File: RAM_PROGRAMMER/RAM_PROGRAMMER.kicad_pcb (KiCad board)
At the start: 4 copper layers, 149.1 x 66 mm, 60 parts, among them J1 Conn_01x02, J2 Conn_01x08, J3 Conn_01x08, J4 Conn_01x08, J5 Conn_01x02, J6 Conn_01x04, J7 Conn_01x11, SW1 SW_Push, U1 ATmega328-PU, U10 74LS245, U2 IS61C1024-15N, U3 74HC595, U4 74LS245, U5 74HC595, U6 74LS157, U7 74LS157, U8 74LS157, U9 74LS157, Y1 Crystal

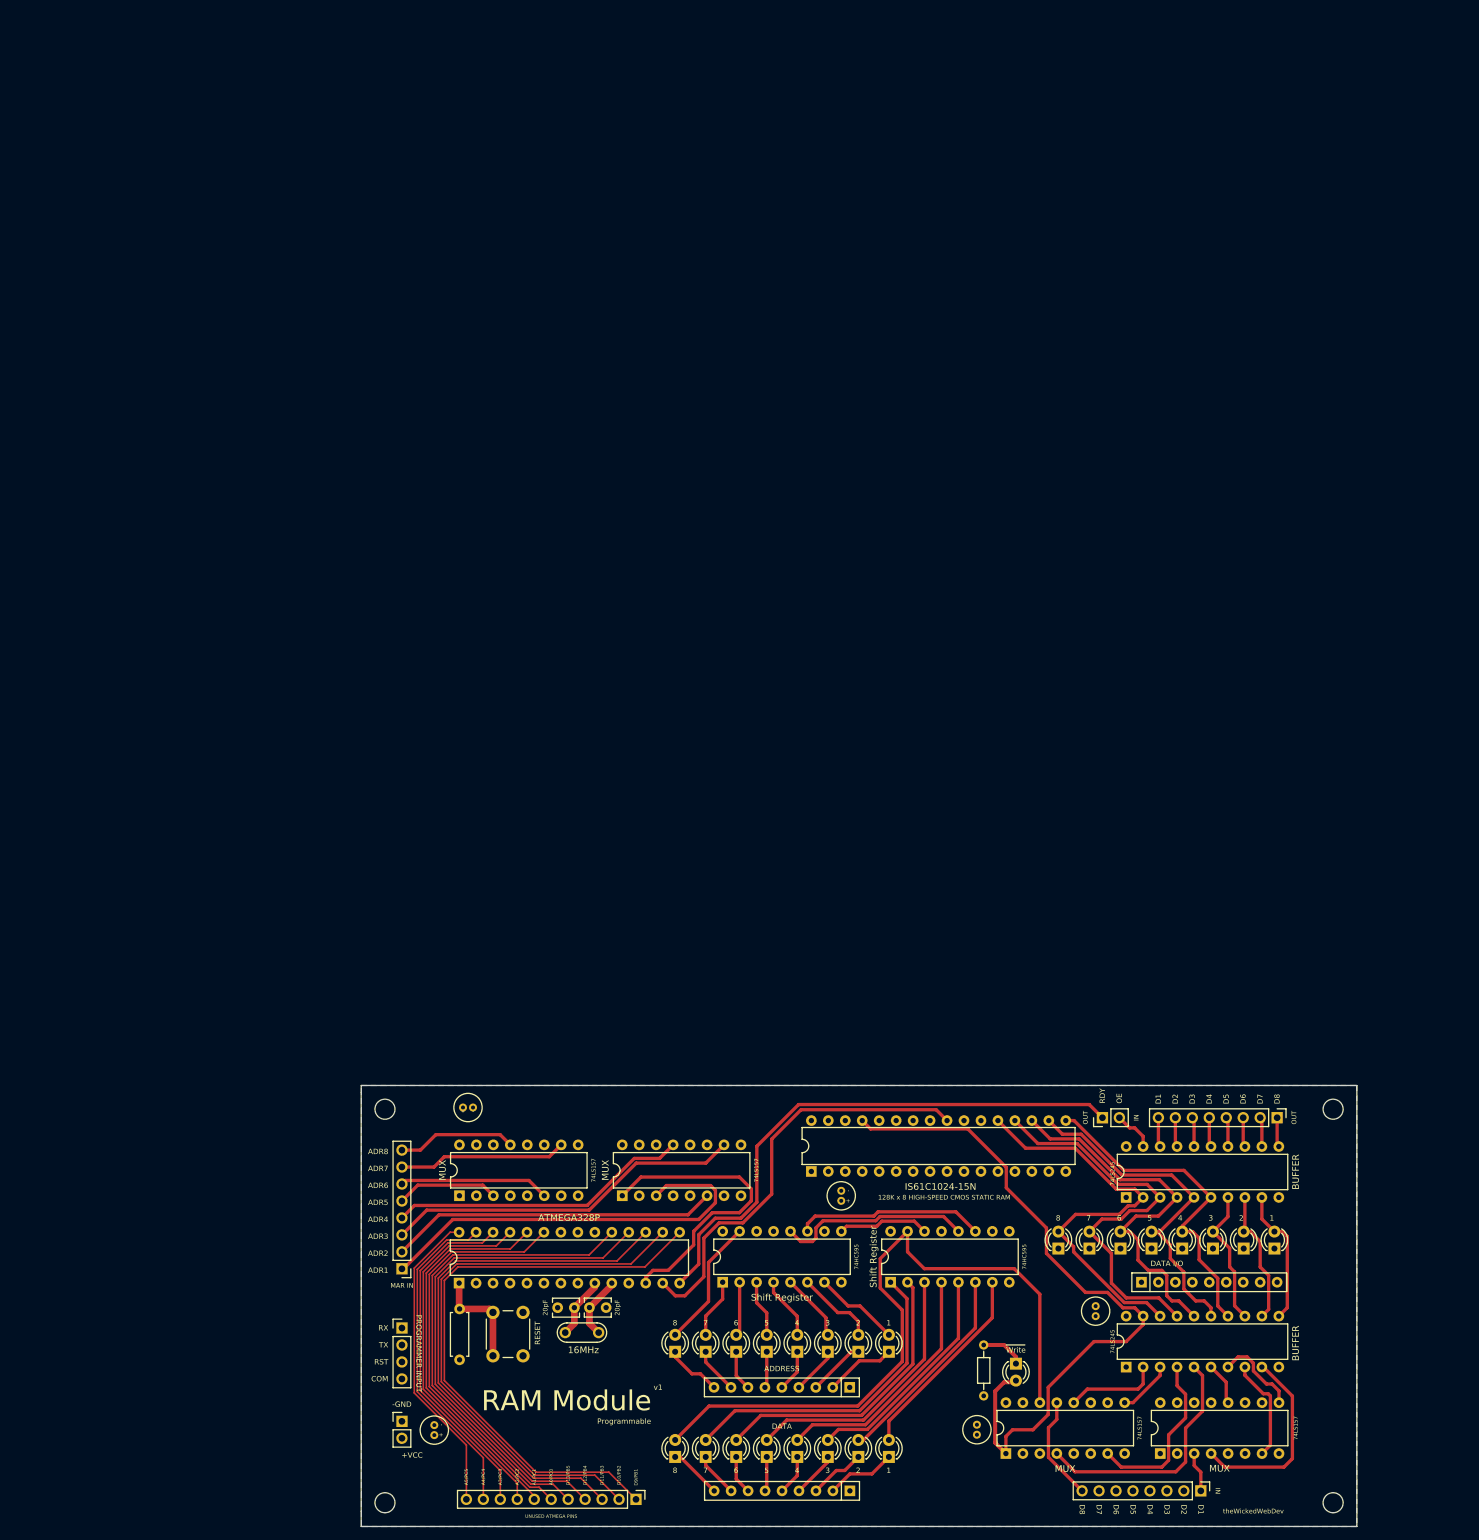
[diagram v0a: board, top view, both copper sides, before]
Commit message: Added RAM Programmer module
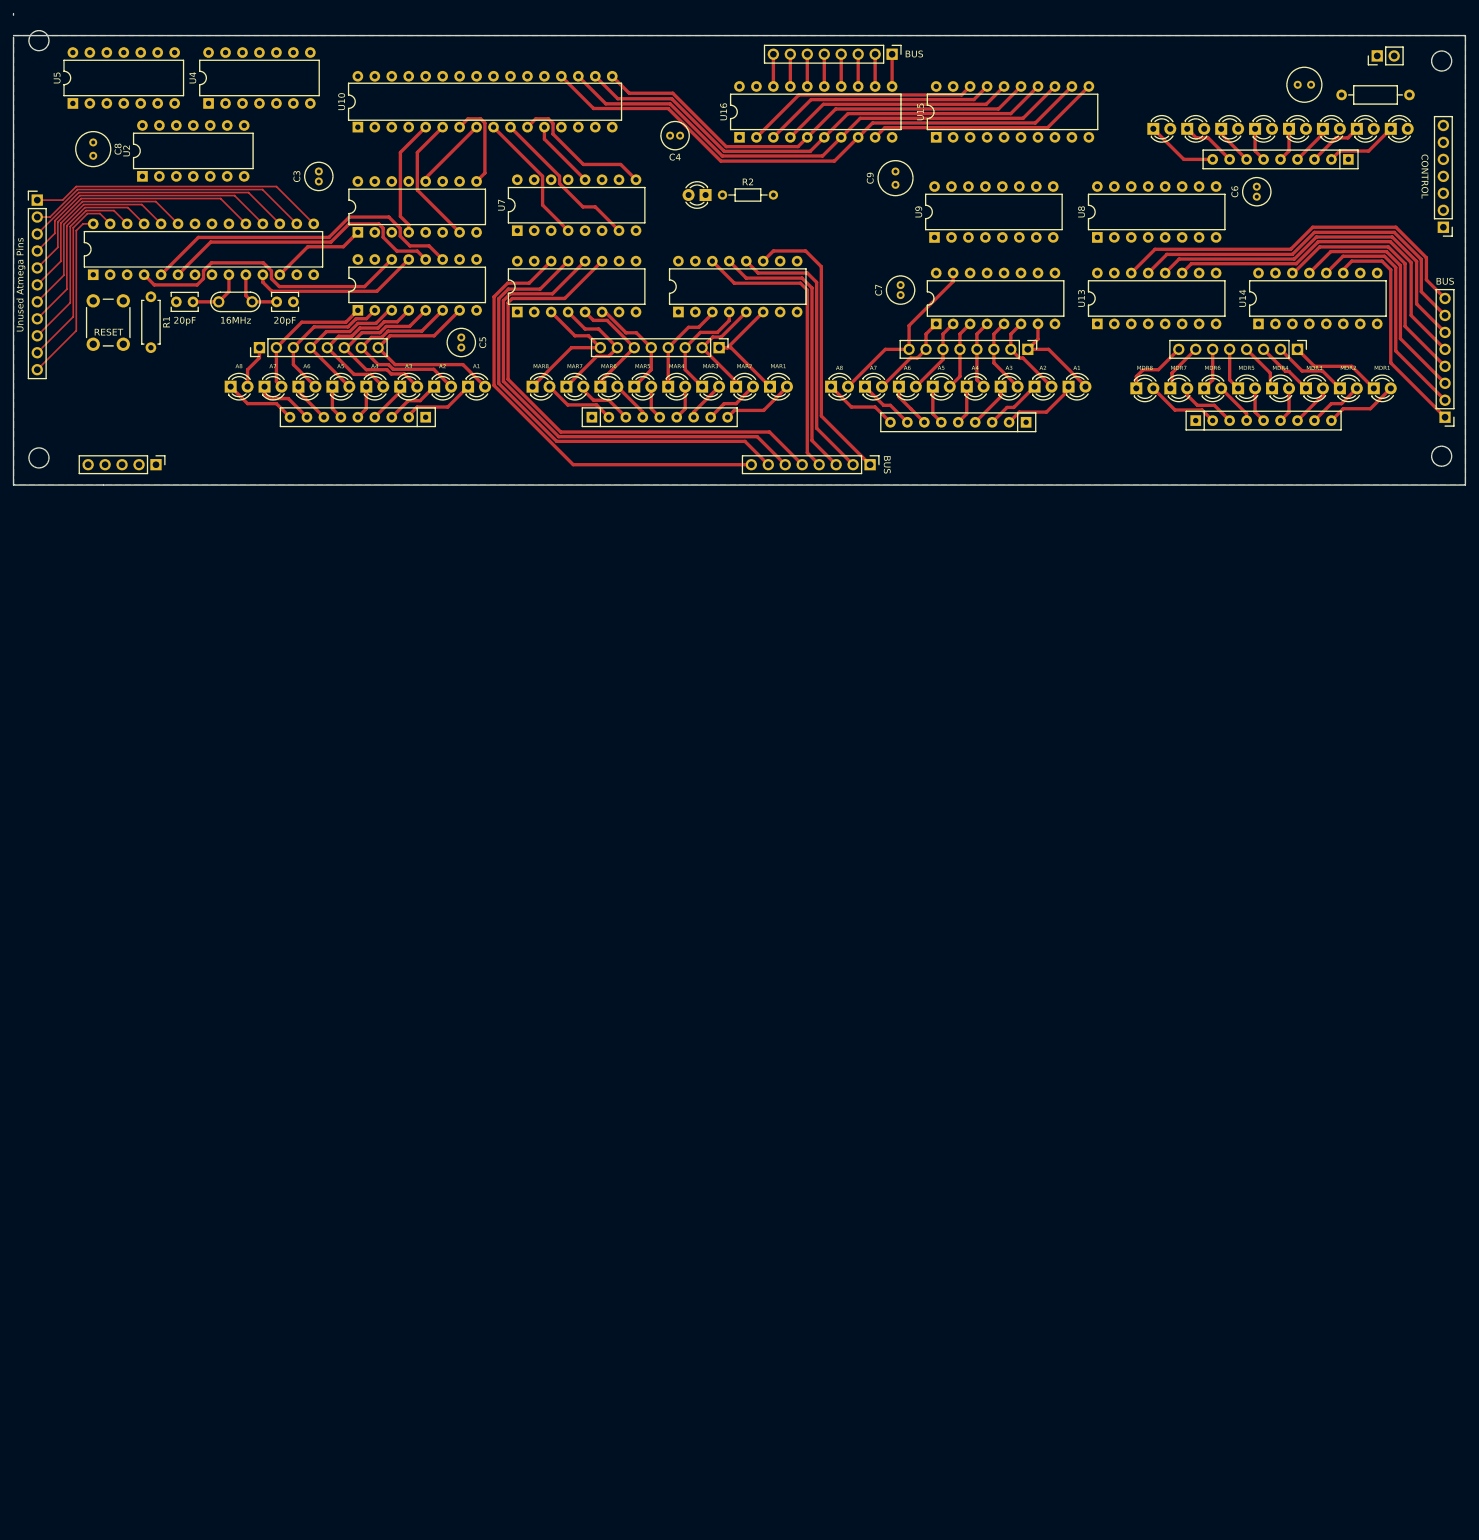
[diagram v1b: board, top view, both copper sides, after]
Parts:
- removed the REF** at (226.5, 79.2)
- removed the REF** at (226.5, 138.2)
- removed the REF** at (84.6, 138.2)
- removed the REF** at (84.6, 79.2)
- added C10: CP_Small, Capacitor_THT:C_Radial_D5.0mm_H7.0mm_P2.00mm, F.Cu at (223.2, -74.2)
- added C8: CP_Small, Capacitor_THT:C_Radial_D5.0mm_H7.0mm_P2.00mm, F.Cu at (40.9, -65.5)
- added C9: CP_Small, Capacitor_THT:C_Radial_D5.0mm_H7.0mm_P2.00mm, F.Cu at (161.0, -59.2)
- added D26: LED, LED_THT:LED_D3.0mm, F.Cu at (197.1, -28.7)
- added D27: LED, LED_THT:LED_D3.0mm, F.Cu at (202.2, -28.7)
- added D28: LED, LED_THT:LED_D3.0mm, F.Cu at (207.2, -28.7)
- added D29: LED, LED_THT:LED_D3.0mm, F.Cu at (212.3, -28.7)
- added D30: LED, LED_THT:LED_D3.0mm, F.Cu at (217.4, -28.7)
- added D31: LED, LED_THT:LED_D3.0mm, F.Cu at (222.5, -28.7)
- added D32: LED, LED_THT:LED_D3.0mm, F.Cu at (227.6, -28.7)
- added D33: LED, LED_THT:LED_D3.0mm, F.Cu at (232.6, -28.7)
- added D34: LED, LED_THT:LED_D3.0mm, F.Cu at (151.4, -29.0)
- added D35: LED, LED_THT:LED_D3.0mm, F.Cu at (156.4, -29.0)
- added D36: LED, LED_THT:LED_D3.0mm, F.Cu at (161.5, -29.0)
- added D37: LED, LED_THT:LED_D3.0mm, F.Cu at (166.6, -29.0)
- added D38: LED, LED_THT:LED_D3.0mm, F.Cu at (171.7, -29.0)
- added D39: LED, LED_THT:LED_D3.0mm, F.Cu at (176.8, -29.0)
- added D40: LED, LED_THT:LED_D3.0mm, F.Cu at (181.8, -29.0)
- added D41: LED, LED_THT:LED_D3.0mm, F.Cu at (186.9, -29.0)
- added J10: Conn_01x08, Connector_PinHeader_2.54mm:PinHeader_1x08_P2.54mm_Vertical, F.Cu at (180.8, -34.5)
- added J11: Conn_01x08, Connector_PinHeader_2.54mm:PinHeader_1x08_P2.54mm_Vertical, F.Cu at (221.2, -34.5)
- added J8: Conn_01x08, Connector_PinHeader_2.54mm:PinHeader_1x08_P2.54mm_Vertical, F.Cu at (157.2, -17.3)
- added J9: Conn_01x08, Connector_PinHeader_2.54mm:PinHeader_1x08_P2.54mm_Vertical, F.Cu at (160.5, -78.7)
- added R4: R_Small_US, Resistor_THT:R_Axial_DIN0207_L6.3mm_D2.5mm_P10.16mm_Horizontal, F.Cu at (238.0, -72.6)
- added REF**: MountingHole_3mm, MountingHole:MountingHole_3mm, F.Cu at (32.7, -18.3)
- added REF**: MountingHole_3mm, MountingHole:MountingHole_3mm, F.Cu at (32.7, -80.8)
- added REF**: MountingHole_3mm, MountingHole:MountingHole_3mm, F.Cu at (242.8, -18.5)
- added REF**: MountingHole_3mm, MountingHole:MountingHole_3mm, F.Cu at (242.8, -77.7)
- added RN4: R_Network08_US, Resistor_THT:R_Array_SIP9, F.Cu at (206.0, -23.9)
- added RN5: R_Network08_US, Resistor_THT:R_Array_SIP9, F.Cu at (180.6, -23.6)
- added U11: 74LS173, Package_DIP:DIP-16_W7.62mm, F.Cu at (104.4, -40.1)
- added U12: 74LS173, Package_DIP:DIP-16_W7.62mm, F.Cu at (128.5, -40.1)
- added U13: 74LS173, Package_DIP:DIP-16_W7.62mm, F.Cu at (191.2, -38.4)
- added U14: 74LS173, Package_DIP:DIP-16_W7.62mm, F.Cu at (215.4, -38.4)
- added U15: 74LS245, Package_DIP:DIP-20_W7.62mm, F.Cu at (167.1, -66.3)
- added U16: 74LS245, Package_DIP:DIP-20_W7.62mm, F.Cu at (137.6, -66.3)
- added U17: 74HC595, Package_DIP:DIP-16_W7.62mm, F.Cu at (167.1, -38.4)
- J2: value Conn_01x08 -> Conn_01x07; footprint Connector_PinHeader_2.54mm:PinHeader_1x08_P2.54mm_Vertical -> Connector_PinHeader_2.54mm:PinHeader_1x07_P2.54mm_Vertical
- J5: value Conn_01x02 -> Conn_01x08; footprint Connector_PinHeader_2.54mm:PinHeader_1x02_P2.54mm_Vertical -> Connector_PinHeader_2.54mm:PinHeader_1x08_P2.54mm_Vertical
- J6: value Conn_01x04 -> Conn_01x05; footprint Connector_PinHeader_2.54mm:PinHeader_1x04_P2.54mm_Vertical -> Connector_PinHeader_2.54mm:PinHeader_1x05_P2.54mm_Vertical
- U10: value 74LS245 -> IS61C1024-15N; footprint Package_DIP:DIP-20_W7.62mm -> Package_DIP:DIP-32_W7.62mm
- U2: value IS61C1024-15N -> 74LS04; footprint Package_DIP:DIP-32_W7.62mm -> Package_DIP:DIP-14_W7.62mm
- U4: value 74LS245 -> 74LS32; footprint Package_DIP:DIP-20_W7.62mm -> Package_DIP:DIP-14_W7.62mm
- U5: value 74HC595 -> 74LS08; footprint Package_DIP:DIP-16_W7.62mm -> Package_DIP:DIP-14_W7.62mm
- moved J1 251.3 mm to (233.1, -78.5), turned to 90 degrees
- moved U4 233.9 mm to (58.1, -71.4)
- moved D9 225.9 mm to (235.2, -67.6), turned to 0 degrees
- moved D11 221.5 mm to (230.1, -67.6), turned to 0 degrees
- moved J2 220.6 mm to (243.1, -52.8)
- moved D13 217.4 mm to (225.0, -67.6), turned to 0 degrees
- moved U5 214.8 mm to (37.8, -71.4)
- moved J7 214.2 mm to (32.5, -56.9), turned to 0 degrees
- moved D15 213.7 mm to (219.9, -67.6), turned to 0 degrees
- moved RN2 212.9 mm to (228.8, -63.0)
- moved D17 210.4 mm to (214.9, -67.6), turned to 0 degrees
- moved D19 207.4 mm to (209.8, -67.6), turned to 0 degrees
- moved D21 204.9 mm to (204.7, -67.6), turned to 0 degrees
- moved D23 202.8 mm to (199.6, -67.6), turned to 0 degrees
- moved U10 197.3 mm to (80.5, -67.8)
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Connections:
- D10 pad 2: /ADR8 -> Net-(D10-Pad2)
- D11 pad 2: /D7 -> Net-(D11-Pad2)
- D12 pad 2: /ADR7 -> Net-(D12-Pad2)
- D13 pad 2: /D6 -> Net-(D13-Pad2)
- D14 pad 2: /ADR6 -> Net-(D14-Pad2)
- D15 pad 2: /D5 -> Net-(D15-Pad2)
- D16 pad 2: /ADR5 -> Net-(D16-Pad2)
- D17 pad 2: /D4 -> Net-(D17-Pad2)
- D18 pad 2: /ADR4 -> Net-(D18-Pad2)
- D19 pad 2: /D3 -> Net-(D19-Pad2)
- D20 pad 2: /ADR3 -> Net-(D20-Pad2)
- D21 pad 2: /D2 -> Net-(D21-Pad2)
- D22 pad 2: /ADR2 -> Net-(D22-Pad2)
- D23 pad 2: /D1 -> Net-(D23-Pad2)
- D24 pad 2: /ADR1 -> Net-(D24-Pad2)
- D25 pad 2: /RAM_WE -> Net-(D25-Pad2)
- D9 pad 2: /D8 -> Net-(D9-Pad2)
- J2 pad 1: /ADR_IN1 -> /CLOCK
- J2 pad 2: /ADR_IN2 -> /RAM_WE
- J2 pad 3: /ADR_IN3 -> /RAM_OUT
- J2 pad 4: /ADR_IN4 -> /MAR_IN
- J2 pad 5: /ADR_IN5 -> /MAR_RST
- J2 pad 6: /ADR_IN6 -> /MEM_IN
- J2 pad 7: /ADR_IN7 -> /MEM_RST
- J3 pad 1: /DATA_IN1 -> Net-(J3-Pad1)
- J3 pad 2: /DATA_IN2 -> Net-(J3-Pad2)
- J3 pad 3: /DATA_IN3 -> Net-(J3-Pad3)
- J3 pad 4: /DATA_IN4 -> Net-(J3-Pad4)
- J3 pad 5: /DATA_IN5 -> Net-(J3-Pad5)
- J3 pad 6: /DATA_IN6 -> Net-(J3-Pad6)
- J3 pad 7: /DATA_IN7 -> Net-(J3-Pad7)
- J3 pad 8: /DATA_IN8 -> Net-(J3-Pad8)
- J4 pad 1: Net-(J4-Pad1) -> Net-(D10-Pad2)
- J4 pad 2: Net-(J4-Pad2) -> Net-(D12-Pad2)
- J4 pad 3: Net-(J4-Pad3) -> Net-(D14-Pad2)
- J4 pad 4: Net-(J4-Pad4) -> Net-(D16-Pad2)
- J4 pad 5: Net-(J4-Pad5) -> Net-(D18-Pad2)
- J4 pad 6: Net-(J4-Pad6) -> Net-(D20-Pad2)
- J4 pad 7: Net-(J4-Pad7) -> Net-(D22-Pad2)
- J4 pad 8: Net-(J4-Pad8) -> Net-(D24-Pad2)
- J5 pad 1: /RAM_READY -> Net-(D8-Pad1)
- J5 pad 2: /RAM_OUT -> Net-(D7-Pad1)
- J6 pad 1: /RX -> /ACTIVE
- J6 pad 2: /TX -> /RX
- J6 pad 3: /RESET -> /TX
- J6 pad 4: GND -> /RESET
- RN1 pad 2: Net-(D1-Pad1) -> Net-(D1-Pad2)
- RN1 pad 3: Net-(D2-Pad1) -> Net-(D2-Pad2)
- RN1 pad 4: Net-(D3-Pad1) -> Net-(D3-Pad2)
- RN1 pad 5: Net-(D4-Pad1) -> Net-(D4-Pad2)
- RN1 pad 6: Net-(D5-Pad1) -> Net-(D5-Pad2)
- RN1 pad 7: Net-(D6-Pad1) -> Net-(D6-Pad2)
- RN1 pad 8: Net-(D7-Pad1) -> Net-(D7-Pad2)
- RN1 pad 9: Net-(D8-Pad1) -> Net-(D8-Pad2)
- RN2 pad 2: Net-(D23-Pad1) -> Net-(D9-Pad1)
- RN2 pad 3: Net-(D21-Pad1) -> Net-(D11-Pad1)
- RN2 pad 4: Net-(D19-Pad1) -> Net-(D13-Pad1)
- RN2 pad 5: Net-(D17-Pad1) -> Net-(D15-Pad1)
- RN2 pad 6: Net-(D15-Pad1) -> Net-(D17-Pad1)
- RN2 pad 7: Net-(D13-Pad1) -> Net-(D19-Pad1)
- RN2 pad 8: Net-(D11-Pad1) -> Net-(D21-Pad1)
- RN2 pad 9: Net-(D9-Pad1) -> Net-(D23-Pad1)
- U1 pad 12: /RAM_WE -> /ENABLE_RAM_WRITE_PROG
- U1 pad 13: /RAM_OE -> /unused?
- U1 pad 14: /RAM_READY -> /ACTIVE
- U10 pad 1: +5V -> Net-(U10-Pad1)
- U10 pad 10: GND -> Net-(U10-Pad10)
- U10 pad 11: Net-(J4-Pad1) -> Net-(U10-Pad11)
- U10 pad 12: Net-(J4-Pad2) -> Net-(U10-Pad12)
- U10 pad 13: Net-(J4-Pad3) -> Net-(D23-Pad2)
- U10 pad 14: Net-(J4-Pad4) -> Net-(D21-Pad2)
- U10 pad 15: Net-(J4-Pad5) -> Net-(D19-Pad2)
- U10 pad 16: Net-(J4-Pad6) -> GND
- U10 pad 17: Net-(J4-Pad7) -> Net-(D17-Pad2)
- U10 pad 18: Net-(J4-Pad8) -> Net-(D15-Pad2)
- U10 pad 19: /RAM_OUT -> Net-(D13-Pad2)
- U10 pad 2: Net-(D1-Pad2) -> GND
- U10 pad 20: +5V -> Net-(D11-Pad2)
- U10 pad 3: Net-(D2-Pad2) -> GND
- U10 pad 4: Net-(D3-Pad2) -> GND
- U10 pad 5: Net-(D4-Pad2) -> Net-(U10-Pad5)
- U10 pad 6: Net-(D5-Pad2) -> Net-(U10-Pad6)
- U10 pad 7: Net-(D6-Pad2) -> Net-(U10-Pad7)
- U10 pad 8: Net-(D7-Pad2) -> Net-(U10-Pad8)
- U10 pad 9: Net-(D8-Pad2) -> Net-(U10-Pad9)
- U2 pad 1: Net-(U2-Pad1) -> Net-(U10-Pad24)
- U2 pad 10: /A3 -> (no net)
- U2 pad 11: /A2 -> (no net)
- U2 pad 12: /A1 -> (no net)
- U2 pad 13: Net-(D8-Pad2) -> (no net)
- U2 pad 14: Net-(D7-Pad2) -> VCC
- U2 pad 2: GND -> Net-(D25-Pad2)
- U2 pad 3: GND -> (no net)
- U2 pad 4: GND -> (no net)
- U2 pad 5: /A8 -> (no net)
- U2 pad 6: /A7 -> (no net)
- U2 pad 7: /A6 -> GND
- U2 pad 8: /A5 -> (no net)
- U2 pad 9: /A4 -> (no net)
- U3 pad 1: /ADR7 -> Net-(D12-Pad2)
- U3 pad 15: /ADR8 -> Net-(D10-Pad2)
- U3 pad 2: /ADR6 -> Net-(D14-Pad2)
- U3 pad 3: /ADR5 -> Net-(D16-Pad2)
- U3 pad 4: /ADR4 -> Net-(D18-Pad2)
- U3 pad 5: /ADR3 -> Net-(D20-Pad2)
- U3 pad 6: /ADR2 -> Net-(D22-Pad2)
- U3 pad 7: /ADR1 -> Net-(D24-Pad2)
- U3 pad 9: Net-(U3-Pad9) -> Net-(U17-Pad14)
- U4 pad 1: +5V -> Net-(U4-Pad1)
- U4 pad 10: GND -> (no net)
- U4 pad 11: Net-(D8-Pad2) -> (no net)
- U4 pad 12: Net-(D7-Pad2) -> (no net)
- U4 pad 13: Net-(D6-Pad2) -> (no net)
- U4 pad 14: Net-(D5-Pad2) -> VCC
- U4 pad 2: /DATA8 -> /ENABLE_RAM_WRITE_PROG
- U4 pad 3: /DATA7 -> Net-(U10-Pad24)
- U4 pad 4: /DATA6 -> (no net)
- U4 pad 5: /DATA5 -> (no net)
- U4 pad 6: /DATA4 -> (no net)
- U4 pad 7: /DATA3 -> GND
- U4 pad 8: /DATA2 -> (no net)
- U4 pad 9: /DATA1 -> (no net)
- U5 pad 1: /D7 -> /CLOCK
- U5 pad 10: +5V -> (no net)
- U5 pad 11: /SH_CLK -> (no net)
- U5 pad 12: /SH_LATCH -> (no net)
- U5 pad 13: /SH_OE -> (no net)
- U5 pad 14: Net-(U3-Pad9) -> (no net)
- U5 pad 2: /D6 -> /RAM_WE
- U5 pad 3: /D5 -> Net-(U4-Pad1)
- U5 pad 4: /D4 -> (no net)
- U5 pad 5: /D3 -> (no net)
- U5 pad 6: /D2 -> (no net)
- U5 pad 7: /D1 -> (no net)
- U5 pad 8: GND -> (no net)
- U5 pad 9: Net-(U5-Pad9) -> (no net)
- U6 pad 1: /RAM_WE -> /ENABLE_RAM_WRITE_PROG
- U6 pad 10: /ADR_IN3 -> Net-(D20-Pad2)
- U6 pad 11: /ADR3 -> Net-(D3-Pad1)
- U6 pad 12: /A4 -> Net-(U10-Pad8)
- U6 pad 13: /ADR_IN4 -> Net-(D18-Pad2)
- U6 pad 14: /ADR4 -> Net-(D4-Pad1)
- U6 pad 2: /ADR1 -> Net-(D1-Pad1)
- U6 pad 3: /ADR_IN1 -> Net-(D24-Pad2)
- U6 pad 4: /A1 -> Net-(U10-Pad5)
- U6 pad 5: /ADR2 -> Net-(D2-Pad1)
- U6 pad 6: /ADR_IN2 -> Net-(D22-Pad2)
- U6 pad 7: /A2 -> Net-(U10-Pad6)
- U6 pad 9: /A3 -> Net-(U10-Pad7)
- U7 pad 1: /RAM_WE -> /ENABLE_RAM_WRITE_PROG
- U7 pad 10: /ADR_IN7 -> Net-(D12-Pad2)
- U7 pad 11: /ADR7 -> Net-(D7-Pad1)
- U7 pad 12: /A8 -> Net-(U10-Pad12)
- U7 pad 13: /ADR_IN8 -> Net-(D10-Pad2)
- U7 pad 14: /ADR8 -> Net-(D8-Pad1)
- U7 pad 2: /ADR5 -> Net-(D5-Pad1)
- U7 pad 3: /ADR_IN5 -> Net-(D16-Pad2)
- U7 pad 4: /A5 -> Net-(U10-Pad9)
- U7 pad 5: /ADR6 -> Net-(D6-Pad1)
- U7 pad 6: /ADR_IN6 -> Net-(D14-Pad2)
- U7 pad 7: /A6 -> Net-(U10-Pad10)
- U7 pad 9: /A7 -> Net-(U10-Pad11)
- U8 pad 1: /PROG_RAM_WE -> /ENABLE_RAM_WRITE_PROG
- U8 pad 10: /DATA_IN3 -> Net-(D39-Pad2)
- U8 pad 11: /D3 -> Net-(D31-Pad1)
- U8 pad 12: /DATA4 -> Net-(U15-Pad6)
- U8 pad 13: /DATA_IN4 -> Net-(D38-Pad2)
- U8 pad 14: /D4 -> Net-(D30-Pad1)
- U8 pad 2: /D1 -> Net-(D33-Pad1)
- U8 pad 3: /DATA_IN1 -> Net-(D41-Pad2)
- U8 pad 4: /DATA1 -> Net-(U15-Pad9)
- U8 pad 5: /D2 -> Net-(D32-Pad1)
- U8 pad 6: /DATA_IN2 -> Net-(D40-Pad2)
- U8 pad 7: /DATA2 -> Net-(U15-Pad8)
- U8 pad 9: /DATA3 -> Net-(U15-Pad7)
- U9 pad 1: /RAM_WE -> /ENABLE_RAM_WRITE_PROG
- U9 pad 10: /DATA_IN7 -> Net-(D35-Pad2)
- U9 pad 11: /D7 -> Net-(D27-Pad1)
- U9 pad 12: /DATA8 -> Net-(U15-Pad2)
- U9 pad 13: /DATA_IN8 -> Net-(D34-Pad2)
- U9 pad 14: /D8 -> Net-(D26-Pad1)
- U9 pad 2: /D5 -> Net-(D29-Pad1)
- U9 pad 3: /DATA_IN5 -> Net-(D37-Pad2)
- U9 pad 4: /DATA5 -> Net-(U15-Pad5)
- U9 pad 5: /D6 -> Net-(D28-Pad1)
- U9 pad 6: /DATA_IN6 -> Net-(D36-Pad2)
- U9 pad 7: /DATA6 -> Net-(U15-Pad4)
- U9 pad 9: /DATA7 -> Net-(U15-Pad3)
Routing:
- net /RAM_WE: track 222.9 -> 0.00 mm
- net /D8: track 103.2 -> 0.00 mm
- net /D7: track 100.2 -> 0.00 mm
- net /D6: track 93.1 -> 0.00 mm
- net /D3: track 91.4 -> 0.00 mm
- net /D4: track 90.3 -> 0.00 mm
- net /D2: track 87.2 -> 0.00 mm
- net Net-(D11-Pad2): track 0.00 -> 86.3 mm
- net /RAM_READY: track 82.7 -> 0.00 mm
- net Net-(D13-Pad2): track 0.00 -> 80.6 mm
- net Net-(J8-Pad5): track 0.00 -> 77.5 mm
- net Net-(D15-Pad2): track 0.00 -> 75.0 mm
- net Net-(J8-Pad6): track 0.00 -> 74.1 mm
- net /D5: track 73.7 -> 0.00 mm
- net /ADR8: track 73.3 -> 0.00 mm
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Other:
- board size 149.1 x 66 mm -> 217.4 x 70.6 mm
- board text added: "A1"
- board text added: "A2"
- board text added: "A3"
- board text added: "A4"
- board text added: "A5"
- board text added: "A6"
- board text added: "A7"
- board text added: "A8"
- board text added: "BUS"
- board text added: "CONTROL"
- board text added: "MAR1"
- board text added: "MAR2"
- board text added: "MAR3"
- board text added: "MAR4"
- board text added: "MAR5"
- board text added: "MAR6"
- board text added: "MAR7"
- board text added: "MAR8"
- board text added: "MDR1"
- board text added: "MDR2"
- board text added: "MDR3"
- board text added: "MDR4"
- board text added: "MDR5"
- board text added: "MDR6"
- board text added: "MDR7"
- board text added: "MDR8"
- board text added: "Unused Atmega Pins"
- board text removed: "+"
- board text removed: "+VCC"
- board text removed: "-"
- board text removed: "-GND"
- board text removed: "1"
- board text removed: "128K x 8 HIGH-SPEED CMOS STATIC RAM"
- board text removed: "2"
- board text removed: "3"
- board text removed: "4"
- board text removed: "5"
- board text removed: "6"
- board text removed: "7"
- board text removed: "74HC595"
- board text removed: "74LS157"
- board text removed: "74LS245"
- board text removed: "8"
- board text removed: "A0/PC0"
- board text removed: "A1/PC1"
- board text removed: "A2/PC2"
- board text removed: "A3/PC3"
- board text removed: "A4/PC4"
- board text removed: "A5/PC5"
- board text removed: "ADDRESS"
- board text removed: "ADR1"
- board text removed: "ADR2"
- board text removed: "ADR3"
- board text removed: "ADR4"
- board text removed: "ADR5"
- board text removed: "ADR6"
- board text removed: "ADR7"
- board text removed: "ADR8"
- board text removed: "ATMEGA328P"
- board text removed: "BUFFER"
- board text removed: "COM"
- board text removed: "D1"
- board text removed: "D10/PB2"
- board text removed: "D11/PB3"
- board text removed: "D12/PB4"
- board text removed: "D13/PB5"
- board text removed: "D2"
- board text removed: "D3"
- board text removed: "D4"
- board text removed: "D5"
- board text removed: "D6"
- board text removed: "D7"
- board text removed: "D8"
- board text removed: "D9/PB1"
- board text removed: "DATA"
- board text removed: "DATA I/O"
- board text removed: "IN"
- board text removed: "IS61C1024-15N"
- board text removed: "MAR IN"
- board text removed: "MUX"
- board text removed: "OE"
- board text removed: "OUT"
- board text removed: "PROGRAMMER INPUT"
- board text removed: "Programmable"
- board text removed: "RAM Module"
- board text removed: "RDY"
- board text removed: "RST"
- board text removed: "RX"
- board text removed: "Shift Register"
- board text removed: "TX"
- board text removed: "UNUSED ATMEGA PINS"
- board text removed: "Write"
- board text removed: "theWickedWebDev"
- board text removed: "v1"
